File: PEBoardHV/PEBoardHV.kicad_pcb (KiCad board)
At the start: 2 copper layers, 106.7 x 76.2 mm, 45 parts, among them J1 To PE LV, J2 Left Connector (Master), J3 E-Meter Internal, J4 Right Connector (Slave), J5 E-Meter External, J6 HV Cable, J7 TSMPs, J8 HV CAN Debug, J9 EMeter HV, U1 L78S05CV-DG, U2 ISO1050, U3 PS2501-4, U4 DK1A1B-12V, U5 DK1A1B-12V

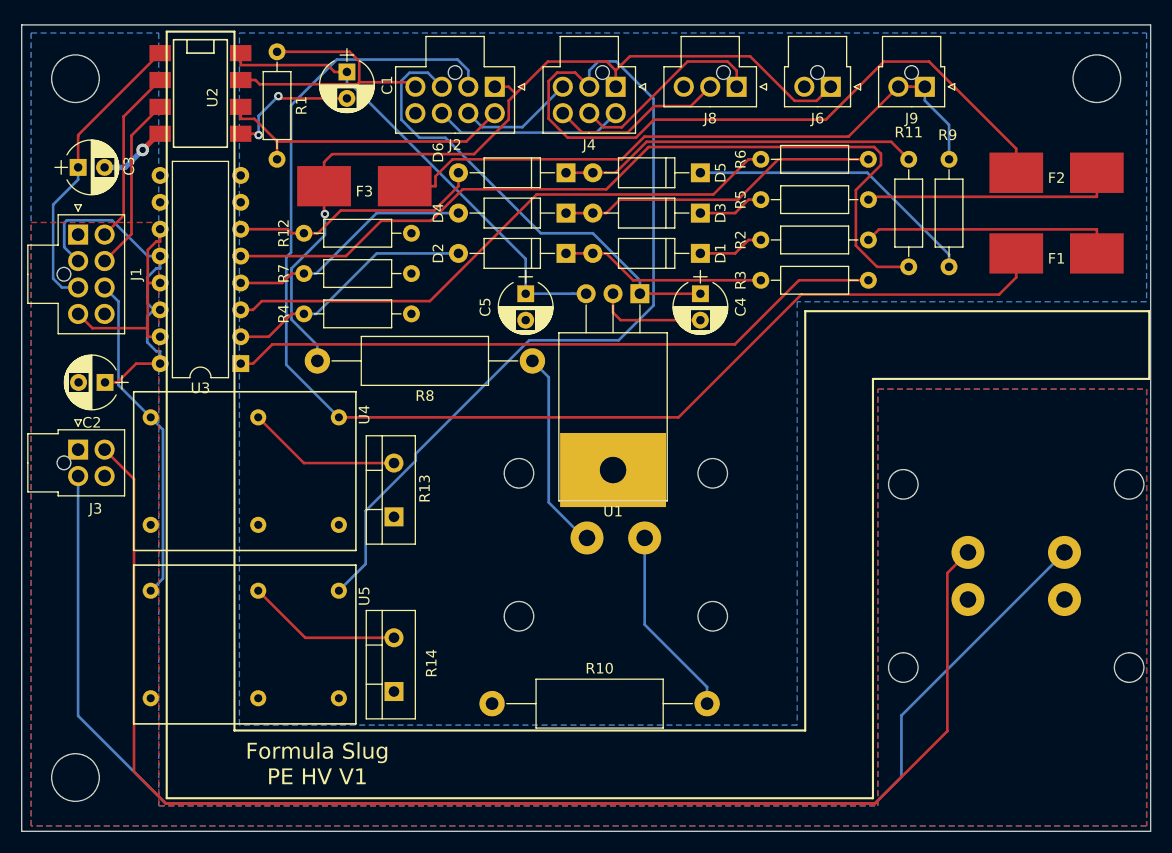
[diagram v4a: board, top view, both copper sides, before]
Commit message: edit PCBs based on actual parts that have arrived
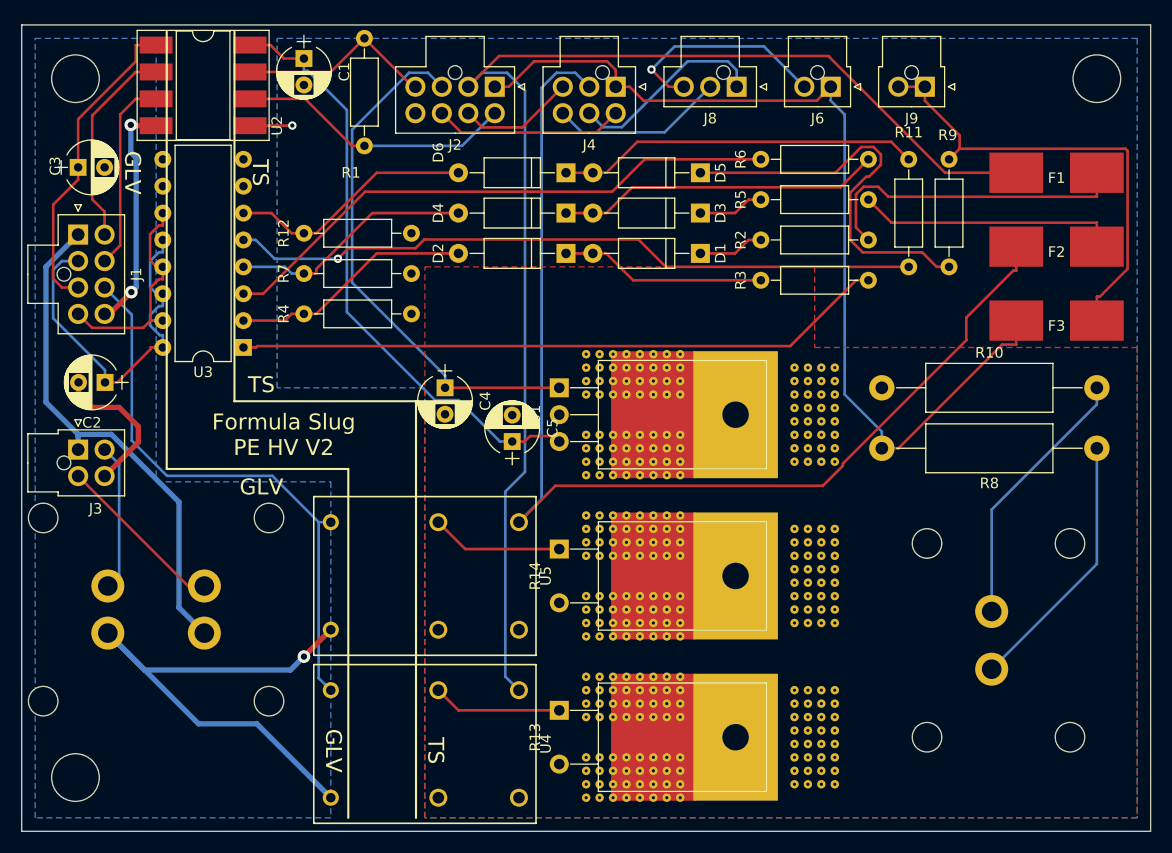
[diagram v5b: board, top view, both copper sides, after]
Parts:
- added V1: ViaBlock, FSFootprints:ViaBlock-0.8mm, F.Cu at (173.7, 124.3)
- added V2: ViaBlock, FSFootprints:ViaBlock-0.8mm, F.Cu at (173.7, 116.7)
- added V3: ViaBlock, FSFootprints:ViaBlock-0.8mm, F.Cu at (173.7, 109.1)
- added V4: ViaBlock, FSFootprints:ViaBlock-0.8mm, F.Cu at (173.7, 101.5)
- added V5: ViaBlock, FSFootprints:ViaBlock-0.8mm, F.Cu at (173.7, 93.9)
- added V6: ViaBlock, FSFootprints:ViaBlock-0.8mm, F.Cu at (173.7, 86.2)
- added V7: ViaBlock, FSFootprints:ViaBlock-0.8mm, F.Cu at (197.2, 123.1)
- added V8: ViaBlock, FSFootprints:ViaBlock-0.8mm, F.Cu at (197.2, 107.8)
- added V9: ViaBlock, FSFootprints:ViaBlock-0.8mm, F.Cu at (197.2, 92.6)
- R13, R14: footprint TO_SOT_Packages_THT:TO-220-2_Vertical -> FSFootprints:TO-220-2_Horizontal_HeatSunk
- U2: footprint SMD_Packages:DIP-8_SMD -> Housings_DIP:DIP-8_W8.89mm_SMDSocket_LongPads
- moved J5 81.3 mm to (133.1, 106.6)
- moved F3 66.6 mm to (218.2, 79.2)
- moved R8 54.0 mm to (222.0, 91.3)
- moved J7 53.3 mm to (219.5, 118.6), turned to 180 degrees
- moved R10 47.4 mm to (201.7, 85.6)
- moved U4 30.9 mm to (159.8, 119.3)
- moved C4 25.7 mm to (160.4, 85.6)
- moved R13 24.1 mm to (171.2, 116.1), turned to 270 degrees
- moved R14 20.6 mm to (171.2, 100.8), turned to 270 degrees
- moved U5 18.2 mm to (159.8, 103.4)
- moved C5 14.0 mm to (166.8, 90.7), turned to 90 degrees
- moved U1 11.7 mm to (171.2, 85.6), turned to 270 degrees
- moved R1 8.35 mm to (152.8, 52.6)
- moved F1 7.62 mm to (218.2, 65.3)
- moved F2 6.98 mm to (218.2, 72.3)
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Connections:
- R13 pad 1: /TS- -> Net-(R13-Pad1)
- R13 pad 2: Net-(R13-Pad2) -> /TS-
- R14 pad 1: /TS- -> Net-(R14-Pad1)
- R14 pad 2: Net-(R14-Pad2) -> /TS-
- U4 pad 6: Net-(R13-Pad2) -> Net-(R13-Pad1)
- U5 pad 6: Net-(R14-Pad2) -> Net-(R14-Pad1)
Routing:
- net /EM_SIG-: track 130.2 -> 13.9 mm
- net /EM_SIG+: track 132.5 -> 16.2 mm
- net GND: track 6.56 -> 87.6 mm, vias 1 -> 3
- net +12V: track 0.00 -> 48.4 mm
- net /TS+_SWITCHED_R: track 135.0 -> 108.1 mm
- net /AIRS_FINAL: track 31.4 -> 53.9 mm
- net /TS+_FUSED: track 61.4 -> 44.5 mm
- net Net-(R11-Pad2): track 80.5 -> 65.4 mm, vias 0 -> 1
- net Net-(R14-Pad2): track 14.7 -> 0.00 mm
- net Net-(R13-Pad2): track 14.6 -> 0.00 mm
- net Net-(R14-Pad1): track 0.00 -> 12.5 mm
- net Net-(R13-Pad1): track 0.00 -> 12.2 mm
- net /5V_TS: track 45.3 -> 57.0 mm
- net Net-(D5-Pad1): track 27.9 -> 38.2 mm
- net /TS+: track 81.0 -> 90.9 mm, vias 1 -> 0
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- added copper zone on F.Cu, net /TS-
- removed copper zone on F.Cu, net +12V
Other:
- board text added: "Formula Slug PE HV V2"
- board text added: "TS GLV"
- board text removed: "Formula Slug PE HV V1"

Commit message: add fuse to CAN+ line on PE HV board
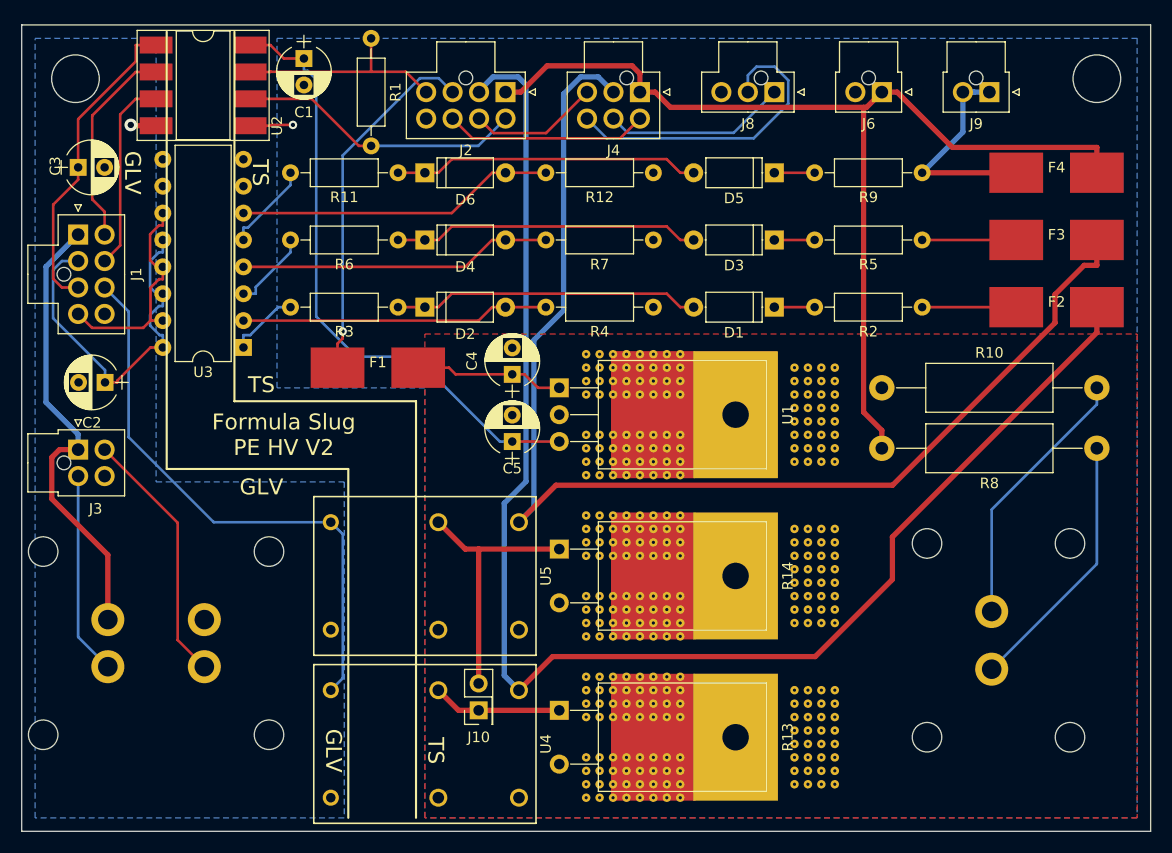
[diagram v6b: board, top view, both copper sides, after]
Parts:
- removed H3: MtngHole, Mounting_Holes:MountingHole_4.5mm
- added F4: Fuse, FSFootprints:SMD Fuse, F.Cu at (218.2, 65.3)
- added J10: Discharge Jumper, Pin_Headers:Pin_Header_Straight_2x01_Pitch2.54mm, F.Cu at (163.6, 116.1)
- D1, D2, D3, D4, D5, D6: footprint Diodes_THT:D_A-405_P10.16mm_Horizontal -> Diodes_THT:D_A-405_P7.62mm_Horizontal
- moved H2 117.0 mm to (222.0, 56.4), turned to 90 degrees
- moved F1 66.7 mm to (154.1, 83.7), turned to 180 degrees
- moved R11 48.3 mm to (156.0, 65.3), turned to 180 degrees
- moved R6 45.1 mm to (156.0, 71.6)
- moved R3 34.4 mm to (156.0, 78.0), turned to 180 degrees
- moved R12 23.6 mm to (180.1, 65.3)
- moved R7 23.1 mm to (180.1, 71.6)
- moved R4 22.9 mm to (180.1, 78.0)
- moved D2 14.3 mm to (158.5, 78.0), turned to 0 degrees
- moved D4 13.6 mm to (158.5, 71.6), turned to 0 degrees
- moved D6 13.3 mm to (158.5, 65.3), turned to 0 degrees
- moved D1 8.64 mm to (191.5, 78.0)
- moved R2 8.13 mm to (205.5, 78.0)
- moved F3 7.62 mm to (218.2, 71.6), turned to 180 degrees
- moved D3 7.43 mm to (191.5, 71.6)
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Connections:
- net Net-(R13-Pad1) renamed /DISCHARGE_L
- net Net-(R14-Pad1) renamed /DISCHARGE_R
- C4 pad 1: /CAN+ -> Net-(C4-Pad1)
- F1 pad 1: /TS+_SWITCHED_L -> Net-(C4-Pad1)
- F1 pad 2: Net-(F1-Pad2) -> /CAN+
- F2 pad 1: /TS+_SWITCHED_R -> /TS+_SWITCHED_L
- F3 pad 1: /TS+ -> /TS+_SWITCHED_R
- F3 pad 2: /TS+_FUSED -> Net-(F3-Pad2)
- R2 pad 1: Net-(F1-Pad2) -> Net-(F2-Pad2)
- R5 pad 1: Net-(F2-Pad2) -> Net-(F3-Pad2)
- U1 pad 1: /CAN+ -> Net-(C4-Pad1)
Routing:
- net GND: track 87.6 -> 2.42 mm, vias 3 -> 1
- net Net-(R11-Pad2): track 65.4 -> 8.44 mm, vias 1 -> 0
- net Net-(R3-Pad2): track 61.7 -> 6.71 mm
- net Net-(R6-Pad2): track 54.2 -> 7.60 mm
- net Net-(D5-Pad1): track 38.2 -> 3.81 mm
- net Net-(F1-Pad2): track 30.5 -> 0.00 mm
- net /TS+_FUSED: track 44.5 -> 20.6 mm
- net /TS-: track 24.6 -> 4.07 mm, vias 2 -> 1
- net Net-(F2-Pad2): track 24.8 -> 8.89 mm
- net /CAN+: track 50.1 -> 34.2 mm, vias 0 -> 1
- net /TS+_SWITCHED_L: track 122.1 -> 137.4 mm
- net Net-(C4-Pad1): track 0.00 -> 14.1 mm
- net /CAN_L_DEBUG: track 16.5 -> 29.6 mm
- net /DISCHARGE_R: track 12.5 -> 25.2 mm
- net /EM_SIG-: track 13.9 -> 24.4 mm
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
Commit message: Tweak 60v circuits based on testing results
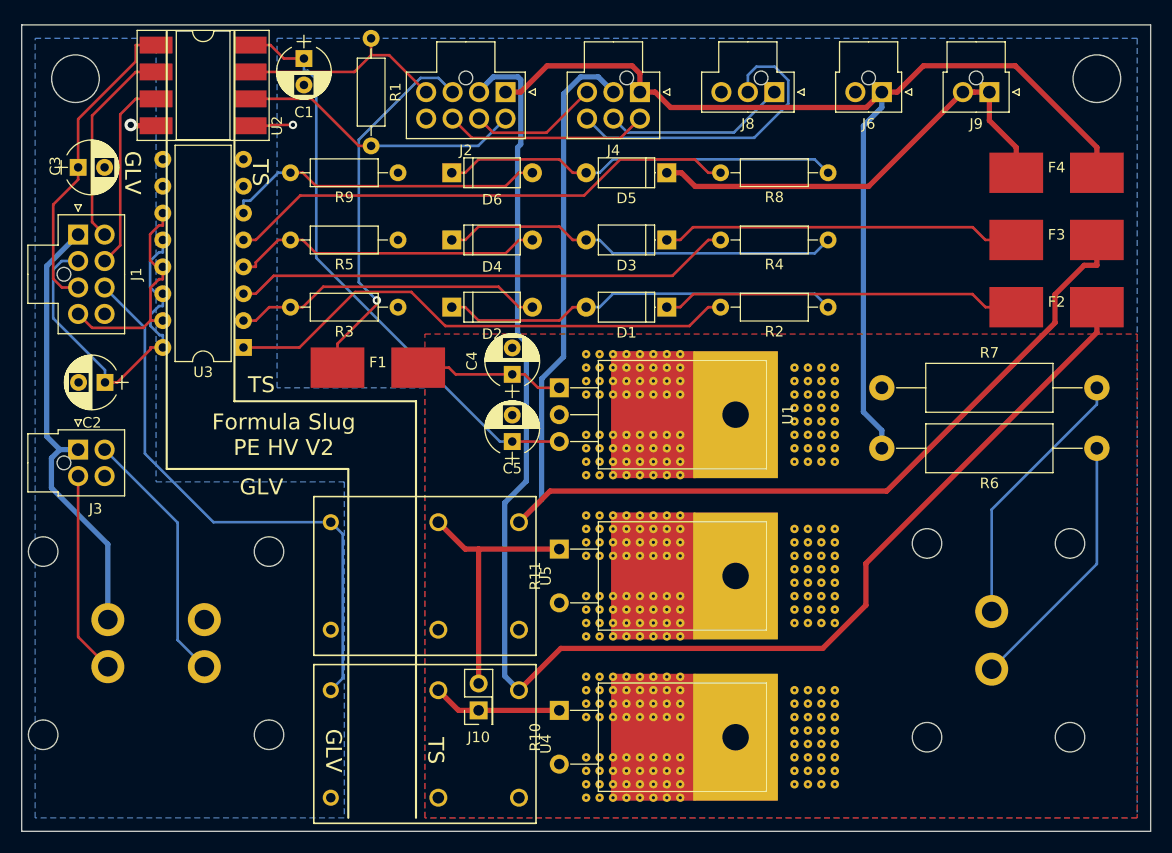
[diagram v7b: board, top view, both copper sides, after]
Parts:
- removed R12: 3kR, Resistors_THT:R_Axial_DIN0207_L6.3mm_D2.5mm_P10.16mm_Horizontal
- removed R13, R14: 1K, FSFootprints:TO-220-2_Horizontal_HeatSunk
- D1, D3, D5: value 48V Zener -> 56V Zener
- R10: value 5kR -> 1K; footprint Resistors_THT:R_Axial_DIN0414_L11.9mm_D4.5mm_P20.32mm_Horizontal -> FSFootprints:TO-220-2_Horizontal_HeatSunk
- R11: value 1.2kR -> 1K; footprint Resistors_THT:R_Axial_DIN0207_L6.3mm_D2.5mm_P10.16mm_Horizontal -> FSFootprints:TO-220-2_Horizontal_HeatSunk
- R2: value R -> 1.2kR
- R3: value 1.2kR -> 1.5k
- R4: value 3kR -> 1.2kR
- R5, R9: value R -> 1.5k
- R6: value 1.2kR -> 5kR; footprint Resistors_THT:R_Axial_DIN0207_L6.3mm_D2.5mm_P10.16mm_Horizontal -> Resistors_THT:R_Axial_DIN0414_L11.9mm_D4.5mm_P20.32mm_Horizontal
- R7: value 3kR -> 5kR; footprint Resistors_THT:R_Axial_DIN0207_L6.3mm_D2.5mm_P10.16mm_Horizontal -> Resistors_THT:R_Axial_DIN0414_L11.9mm_D4.5mm_P20.32mm_Horizontal
- R8: value 5kR -> 1.2kR; footprint Resistors_THT:R_Axial_DIN0414_L11.9mm_D4.5mm_P20.32mm_Horizontal -> Resistors_THT:R_Axial_DIN0207_L6.3mm_D2.5mm_P10.16mm_Horizontal
- moved R6 68.9 mm to (222.0, 91.3)
- moved R5 49.5 mm to (156.0, 71.6)
- moved R9 49.5 mm to (156.0, 65.3)
- moved R10 43.1 mm to (171.2, 116.1), turned to 270 degrees
- moved R11 38.7 mm to (171.2, 100.8), turned to 270 degrees
- moved R8 36.4 mm to (196.6, 65.3)
- moved R7 25.7 mm to (201.7, 85.6), turned to 0 degrees
- moved R4 17.7 mm to (196.6, 71.6)
- moved D1 10.2 mm to (181.4, 78.0)
- moved D3 10.2 mm to (181.4, 71.6)
- moved D5 10.2 mm to (181.4, 65.3)
- moved R2 8.89 mm to (196.6, 78.0)
- moved D2 2.54 mm to (161.0, 78.0)
- moved D4 2.54 mm to (161.0, 71.6)
- moved D6 2.54 mm to (161.0, 65.3)
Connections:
- D5 pad 1: Net-(D5-Pad1) -> /TS+_FUSED
- F2 pad 2: Net-(F2-Pad2) -> Net-(D1-Pad1)
- F3 pad 2: Net-(F3-Pad2) -> Net-(D3-Pad1)
- R10 pad 1: /TS- -> /DISCHARGE_L
- R10 pad 2: Net-(J7-Pad2) -> /TS-
- R11 pad 1: Net-(D5-Pad2) -> /DISCHARGE_R
- R11 pad 2: Net-(R11-Pad2) -> /TS-
- R2 pad 1: Net-(F2-Pad2) -> Net-(D1-Pad2)
- R2 pad 2: Net-(D1-Pad1) -> Net-(R2-Pad2)
- R3 pad 1: Net-(D1-Pad2) -> /TS-
- R3 pad 2: Net-(R3-Pad2) -> Net-(D2-Pad2)
- R4 pad 1: /TS- -> Net-(D3-Pad2)
- R4 pad 2: Net-(D2-Pad2) -> Net-(R4-Pad2)
- R5 pad 1: Net-(F3-Pad2) -> /TS-
- R5 pad 2: Net-(D3-Pad1) -> Net-(D4-Pad2)
- R6 pad 1: Net-(D3-Pad2) -> Net-(J7-Pad1)
- R6 pad 2: Net-(R6-Pad2) -> /TS+
- R7 pad 2: Net-(D4-Pad2) -> Net-(J7-Pad2)
- R8 pad 1: Net-(J7-Pad1) -> Net-(D5-Pad2)
- R8 pad 2: /TS+ -> Net-(R8-Pad2)
- R9 pad 1: /TS+_FUSED -> /TS-
- R9 pad 2: Net-(D5-Pad1) -> Net-(D6-Pad2)
- U3 pad 1: Net-(R3-Pad2) -> Net-(R2-Pad2)
- U3 pad 3: Net-(R6-Pad2) -> Net-(R4-Pad2)
- U3 pad 5: Net-(R11-Pad2) -> Net-(R8-Pad2)
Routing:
- net Net-(R2-Pad2): track 0.00 -> 49.3 mm
- net Net-(R8-Pad2): track 0.00 -> 48.8 mm
- net Net-(R4-Pad2): track 0.00 -> 47.2 mm
- net Net-(D1-Pad1): track 3.81 -> 34.0 mm
- net Net-(D3-Pad1): track 3.81 -> 34.0 mm
- net /TS+_FUSED: track 20.6 -> 43.4 mm
- net Net-(F3-Pad2): track 8.89 -> 0.00 mm
- net Net-(F2-Pad2): track 8.89 -> 0.00 mm
- net Net-(D1-Pad2): track 29.0 -> 37.7 mm
- net Net-(D3-Pad2): track 29.0 -> 37.7 mm
- net Net-(D5-Pad2): track 29.0 -> 37.7 mm
- net Net-(R11-Pad2): track 8.44 -> 0.00 mm
- net Net-(R6-Pad2): track 7.60 -> 0.00 mm
- net Net-(R3-Pad2): track 6.71 -> 0.00 mm
- net /TS+: track 97.6 -> 101.9 mm
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
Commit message: Add TVS diode and choke to PE HV board
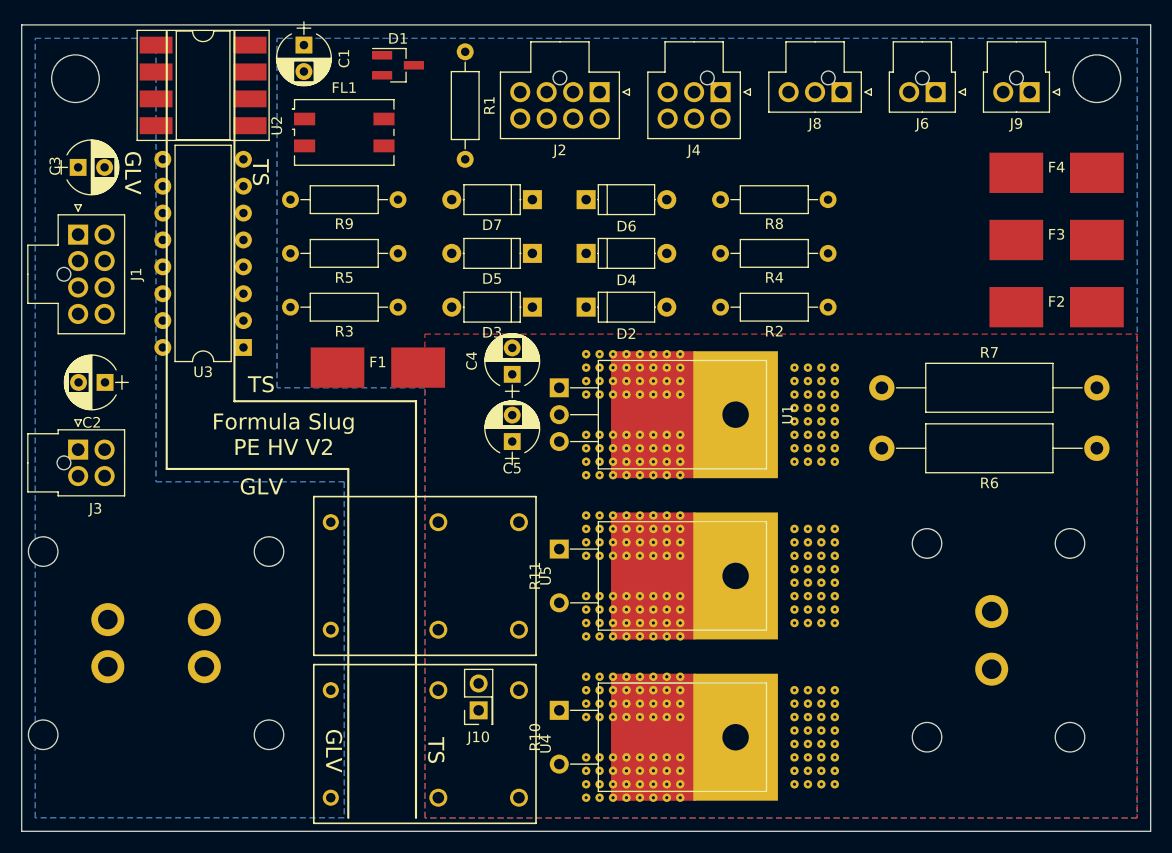
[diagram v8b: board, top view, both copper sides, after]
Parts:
- added D7: 12V Zener, Diodes_THT:D_A-405_P7.62mm_Horizontal, F.Cu at (168.7, 67.8)
- added FL1: EMI_Choke, FSFootprints:L_CommonMode_Choke, F.Cu at (150.9, 61.5)
- D1: value 56V Zener -> D_TVS_x2_AAC; footprint Diodes_THT:D_A-405_P7.62mm_Horizontal -> TO_SOT_Packages_SMD:SOT-23_Handsoldering
- D2, D4, D6: value 12V Zener -> 56V Zener
- D3, D5: value 56V Zener -> 12V Zener
- moved D1 34.2 mm to (156.0, 55.1), turned to 0 degrees
- moved D5 14.8 mm to (168.7, 72.9)
- moved D3 14.2 mm to (168.7, 78.0)
- moved D6 13.0 mm to (173.7, 67.8)
- moved D4 12.8 mm to (173.7, 72.9)
- moved D2 12.7 mm to (173.7, 78.0)
- moved R1 8.98 mm to (162.3, 53.8)
- moved J2 8.89 mm to (175.0, 57.7)
- moved J4 7.62 mm to (186.4, 57.7)
- moved J8 6.35 mm to (197.9, 57.7)
- moved J6 5.08 mm to (206.8, 57.7)
- moved J9 3.81 mm to (215.6, 57.7)
- moved R8 2.54 mm to (196.6, 67.8)
- moved R9 2.54 mm to (156.0, 67.8)
- moved C1 1.27 mm to (147.1, 53.2)
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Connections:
- D1 pad 1: Net-(D1-Pad1) -> /CAN_H_BOARD
- D1 pad 2: Net-(D1-Pad2) -> /CAN_L_BOARD
- D2 pad 1: Net-(D1-Pad2) -> Net-(D2-Pad1)
- D3 pad 1: Net-(D3-Pad1) -> Net-(D2-Pad2)
- D4 pad 1: Net-(D3-Pad2) -> Net-(D4-Pad1)
- D5 pad 1: /TS+_FUSED -> Net-(D4-Pad2)
- D6 pad 1: Net-(D5-Pad2) -> /TS+_FUSED
- F2 pad 2: Net-(D1-Pad1) -> Net-(D2-Pad1)
- F3 pad 2: Net-(D3-Pad1) -> Net-(D4-Pad1)
- R2 pad 1: Net-(D1-Pad2) -> Net-(D2-Pad2)
- R3 pad 2: Net-(D2-Pad2) -> Net-(D3-Pad2)
- R4 pad 1: Net-(D3-Pad2) -> Net-(D4-Pad2)
- R5 pad 2: Net-(D4-Pad2) -> Net-(D5-Pad2)
- R8 pad 1: Net-(D5-Pad2) -> Net-(D6-Pad2)
- R9 pad 2: Net-(D6-Pad2) -> Net-(D7-Pad2)
- U2 pad 6: /CAN_L_BOARD -> /CAN_L_PRE
- U2 pad 7: /CAN_H_BOARD -> /CAN_H_PRE
- U3 pad 2: Net-(D2-Pad2) -> Net-(D3-Pad2)
- U3 pad 4: Net-(D4-Pad2) -> Net-(D5-Pad2)
- U3 pad 6: Net-(D6-Pad2) -> Net-(D7-Pad2)
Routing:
- net /TS+_SWITCHED_L: track 137.6 -> 0.00 mm
- net /TS+_SWITCHED_R: track 116.8 -> 0.00 mm
- net /TS+: track 101.9 -> 0.00 mm
- net /5V_TS: track 55.3 -> 0.00 mm
- net /AIRS_FINAL: track 54.3 -> 0.00 mm
- net Net-(R2-Pad2): track 49.3 -> 0.00 mm
- net Net-(R8-Pad2): track 48.8 -> 0.00 mm
- net Net-(R4-Pad2): track 47.2 -> 0.00 mm
- net /TS+_FUSED: track 43.4 -> 0.00 mm
- net +12V: track 42.4 -> 0.00 mm
- net Net-(D5-Pad2): track 37.7 -> 0.00 mm
- net Net-(D1-Pad2): track 37.7 -> 0.00 mm
- net Net-(D3-Pad2): track 37.7 -> 0.00 mm
- net /CAN+: track 35.6 -> 0.00 mm, vias 1 -> 0
- net /5V_GLV: track 35.6 -> 0.00 mm
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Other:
- net class HighSpeed added: clearance 0.24, trace_width 0.25, via_dia 100, via_drill 0.4
